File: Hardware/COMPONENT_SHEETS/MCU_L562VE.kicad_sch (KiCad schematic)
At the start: 29 parts, among them SW1 MCU Reset, U9 STM32L562VET6Q, Y2 32MHz

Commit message: wtf is wrong with my github install
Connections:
- net ABORT_1: now also U9.37 (PE9); no longer U9.62 (PD15)
- net ABORT_2: now also U9.38 (PE10); no longer U9.61 (PD14)
- net SPI1_MISO: now also U9.53 (PB14); no longer U9.30 (PA6)
- net SPI1_MOSI: now also U9.54 (PB15); no longer U9.31 (PA7)
- net SPI1_SCK: now also U9.52 (PB13); no longer U9.29 (PA5)
- net SPI2_MISO: now also U9.30 (PA6); no longer U9.53 (PB14)
- net SPI2_MOSI: now also U9.31 (PA7); no longer U9.54 (PB15)
- net SPI2_SCK: now also U9.29 (PA5); no longer U9.52 (PB13)
- net at U9.35 (PE7): no longer D2.2 (A)
- net at U9.36 (PE8): no longer D3.2 (A)
- net at D4.2 (A): no longer U9.37 (PE9)
- net at D5.2 (A): no longer U9.38 (PE10)
- net at U9.39 (PE11): no longer D6.2 (A)
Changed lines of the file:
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@@
-    (stroke (width 0) (type default) (color 0 0 0 0))
-  )
-  (wire (pts (xy 77.47 111.76) (xy 52.07 111.76))
     (stroke (width 0) (type default) (color 0 0 0 0))
   )
@@
     (stroke (width 0) (type default) (color 0 0 0 0))
   )
-  (wire (pts (xy 77.47 109.22) (xy 44.45 109.22))
-    (stroke (width 0) (type default) (color 0 0 0 0))
-  )
   (wire (pts (xy 97.79 172.72) (xy 97.79 173.99))
     (stroke (width 0) (type default) (color 0 0 0 0))
@@
     (stroke (width 0) (type default) (color 0 0 0 0))
   )
-  (wire (pts (xy 77.47 101.6) (xy 21.59 101.6))
-    (stroke (width 0) (type default) (color 0 0 0 0))
-  )
   (wire (pts (xy 102.87 33.02) (xy 102.87 31.75))
     (stroke (width 0) (type default) (color 0 0 0 0))
@@
     (stroke (width 0) (type default) (color 0 0 0 0))
   )
-  (wire (pts (xy 77.47 106.68) (xy 36.83 106.68))
-    (stroke (width 0) (type default) (color 0 0 0 0))
-  )
   (wire (pts (xy 44.45 123.19) (xy 44.45 125.73))
     (stroke (width 0) (type default) (color 0 0 0 0))
@@
   )
   (wire (pts (xy 189.23 34.29) (xy 189.23 35.56))
-    (stroke (width 0) (type default) (color 0 0 0 0))
-  )
-  (wire (pts (xy 77.47 104.14) (xy 29.21 104.14))
     (stroke (width 0) (type default) (color 0 0 0 0))
   )
@@
     (effects (font (size 1.27 1.27)) (justify left))
   )
-  (hierarchical_label "ABORT_1" (shape input) (at 77.47 165.1 180)
-    (effects (font (size 1.27 1.27)) (justify right))
-  )
-  (hierarchical_label "SPI2_MISO" (shape input) (at 123.19 119.38 0)
-    (effects (font (size 1.27 1.27)) (justify left))
-  )
-  (hierarchical_label "SPI2_SCK" (shape input) (at 123.19 116.84 0)
+  (hierarchical_label "ABORT_1" (shape input) (at 77.47 106.68 180)
+    (effects (font (size 1.27 1.27)) (justify right))
+  )
+  (hierarchical_label "SPI2_MISO" (shape input) (at 123.19 55.88 0)
+    (effects (font (size 1.27 1.27)) (justify left))
+  )
+  (hierarchical_label "SPI2_SCK" (shape input) (at 123.19 53.34 0)
     (effects (font (size 1.27 1.27)) (justify left))
   )
@@
     (effects (font (size 1.27 1.27)) (justify left))
   )
-  (hierarchical_label "ABORT_2" (shape input) (at 77.47 162.56 180)
-    (effects (font (size 1.27 1.27)) (justify right))
-  )
-  (hierarchical_label "SPI2_MOSI" (shape input) (at 123.19 121.92 0)
-    (effects (font (size 1.27 1.27)) (justify left))
-  )
-  (hierarchical_label "SPI1_MISO" (shape input) (at 123.19 55.88 0)
+  (hierarchical_label "ABORT_2" (shape input) (at 77.47 109.22 180)
+    (effects (font (size 1.27 1.27)) (justify right))
+  )
+  (hierarchical_label "SPI2_MOSI" (shape input) (at 123.19 58.42 0)
+    (effects (font (size 1.27 1.27)) (justify left))
+  )
+  (hierarchical_label "SPI1_MISO" (shape input) (at 123.19 119.38 0)
     (effects (font (size 1.27 1.27)) (justify left))
   )
@@
     (effects (font (size 1.27 1.27)) (justify left))
   )
-  (hierarchical_label "SPI1_SCK" (shape input) (at 123.19 53.34 0)
+  (hierarchical_label "SPI1_SCK" (shape input) (at 123.19 116.84 0)
     (effects (font (size 1.27 1.27)) (justify left))
   )
@@
     (effects (font (size 1.27 1.27)) (justify right))
   )
-  (hierarchical_label "SPI1_MOSI" (shape input) (at 123.19 58.42 0)
-    (effects (font (size 1.27 1.27)) (justify left))
-  )
+  (hierarchical_label "SPI1_MOSI" (shape input) (at 123.19 121.92 0)
+    (effects (font (size 1.27 1.27)) (justify left))
+  )

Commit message: almost there
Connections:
- net GND: now also D2.1 (K), D3.1 (K), D4.1 (K), D5.1 (K), D6.1 (K); no longer R10.1, R6.1, R7.1, R8.1, R9.1
- net at R10.2: no longer D6.1 (K)
- net at D6.2 (A): now also R10.1
- net at R9.2: no longer D5.1 (K)
- net at D5.2 (A): now also R9.1
- net at R8.2: no longer D4.1 (K)
- net at D4.2 (A): now also R8.1
- net at R7.2: no longer D3.1 (K)
- net at D3.2 (A): now also R7.1
- net at R6.2: no longer D2.1 (K)
- net at D2.2 (A): now also R6.1
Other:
- moved on the sheet: R10, R6, R7, R8, R9
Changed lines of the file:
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@@
-    (stroke (width 0) (type default) (color 0 0 0 0))
-  )
-  (wire (pts (xy 44.45 109.22) (xy 44.45 118.11))
     (stroke (width 0) (type default) (color 0 0 0 0))
   )
@@
     (stroke (width 0) (type default) (color 0 0 0 0))
   )
-  (wire (pts (xy 29.21 123.19) (xy 29.21 125.73))
+  (wire (pts (xy 29.21 123.19) (xy 29.21 130.81))
     (stroke (width 0) (type default) (color 0 0 0 0))
   )
@@
     (stroke (width 0) (type default) (color 0 0 0 0))
   )
-  (wire (pts (xy 52.07 118.11) (xy 52.07 111.76))
-    (stroke (width 0) (type default) (color 0 0 0 0))
-  )
   (wire (pts (xy 189.23 40.64) (xy 189.23 41.91))
     (stroke (width 0) (type default) (color 0 0 0 0))
@@
     (stroke (width 0) (type default) (color 0 0 0 0))
   )
-  (wire (pts (xy 21.59 118.11) (xy 21.59 101.6))
-    (stroke (width 0) (type default) (color 0 0 0 0))
-  )
   (wire (pts (xy 107.95 31.75) (xy 110.49 31.75))
     (stroke (width 0) (type default) (color 0 0 0 0))
@@
     (stroke (width 0) (type default) (color 0 0 0 0))
   )
-  (wire (pts (xy 21.59 123.19) (xy 21.59 125.73))
+  (wire (pts (xy 21.59 123.19) (xy 21.59 130.81))
     (stroke (width 0) (type default) (color 0 0 0 0))
   )
@@
     (stroke (width 0) (type default) (color 0 0 0 0))
   )
+  (wire (pts (xy 52.07 114.3) (xy 52.07 118.11))
+    (stroke (width 0) (type default) (color 0 0 0 0))
+  )
   (wire (pts (xy 102.87 33.02) (xy 102.87 31.75))
     (stroke (width 0) (type default) (color 0 0 0 0))
@@
     (stroke (width 0) (type default) (color 0 0 0 0))
   )
-  (wire (pts (xy 29.21 118.11) (xy 29.21 104.14))
-    (stroke (width 0) (type default) (color 0 0 0 0))
-  )
   (wire (pts (xy 95.25 31.75) (xy 97.79 31.75))
     (stroke (width 0) (type default) (color 0 0 0 0))
@@
     (stroke (width 0) (type default) (color 0 0 0 0))
   )
-  (wire (pts (xy 44.45 123.19) (xy 44.45 125.73))
+  (wire (pts (xy 44.45 123.19) (xy 44.45 130.81))
     (stroke (width 0) (type default) (color 0 0 0 0))
   )
@@
     (stroke (width 0) (type default) (color 0 0 0 0))
   )
+  (wire (pts (xy 44.45 114.3) (xy 44.45 118.11))
+    (stroke (width 0) (type default) (color 0 0 0 0))
+  )
   (wire (pts (xy 223.52 40.64) (xy 223.52 41.91))
     (stroke (width 0) (type default) (color 0 0 0 0))
@@
     (stroke (width 0) (type default) (color 0 0 0 0))
   )
-  (wire (pts (xy 36.83 123.19) (xy 36.83 125.73))
+  (wire (pts (xy 36.83 114.3) (xy 36.83 118.11))
+    (stroke (width 0) (type default) (color 0 0 0 0))
+  )
+  (wire (pts (xy 36.83 123.19) (xy 36.83 130.81))
     (stroke (width 0) (type default) (color 0 0 0 0))
   )
@@
     (stroke (width 0) (type default) (color 0 0 0 0))
   )
-  (wire (pts (xy 52.07 123.19) (xy 52.07 125.73))
+  (wire (pts (xy 52.07 123.19) (xy 52.07 130.81))
     (stroke (width 0) (type default) (color 0 0 0 0))
   )
@@
     (stroke (width 0) (type default) (color 0 0 0 0))
   )
-  (wire (pts (xy 36.83 118.11) (xy 36.83 106.68))
+  (wire (pts (xy 21.59 114.3) (xy 21.59 118.11))
     (stroke (width 0) (type default) (color 0 0 0 0))
   )
@@
   )
   (wire (pts (xy 90.17 31.75) (xy 90.17 33.02))
+    (stroke (width 0) (type default) (color 0 0 0 0))
+  )
+  (wire (pts (xy 29.21 114.3) (xy 29.21 118.11))
     (stroke (width 0) (type default) (color 0 0 0 0))
   )
@@
     (pin "2")
   )
-  (symbol (lib_id "Device:R_Small") (at 21.59 128.27 180) (unit 1)
-    (in_bom yes) (on_board yes)
-    (property "Reference" "R6" (id 0) (at 24.13 129.54 0))
-    (property "Value" "820" (id 1) (at 25.4 127 0))
-    (property "Footprint" "Resistor_SMD:R_0603_1608Metric_Pad0.98x0.95mm_HandSolder" (id 2) (at 21.59 128.27 0)
-      (effects (font (size 1.27 1.27)) hide)
-    )
-    (property "Datasheet" "~" (id 3) (at 21.59 128.27 0)
-      (effects (font (size 1.27 1.27)) hide)
-    )
-    (property "LCSC" " C23253" (id 4) (at 21.59 128.27 0)
-      (effects (font (size 1.27 1.27)) hide)
-    )
-    (pin "1")
-    (pin "2")
-  )
-  (symbol (lib_id "Device:R_Small") (at 36.83 128.27 180) (unit 1)
-    (in_bom yes) (on_board yes)
-    (property "Reference" "R8" (id 0) (at 39.37 129.54 0))
-    (property "Value" "820" (id 1) (at 40.64 127 0))
-    (property "Footprint" "Resistor_SMD:R_0603_1608Metric_Pad0.98x0.95mm_HandSolder" (id 2) (at 36.83 128.27 0)
-      (effects (font (size 1.27 1.27)) hide)
-    )
-    (property "Datasheet" "~" (id 3) (at 36.83 128.27 0)
-      (effects (font (size 1.27 1.27)) hide)
-    )
-    (property "LCSC" " C23253 " (id 4) (at 36.83 128.27 0)
-      (effects (font (size 1.27 1.27)) hide)
-    )
-    (pin "1")
-    (pin "2")
-  )
-  (symbol (lib_id "Device:R_Small") (at 52.07 128.27 180) (unit 1)
-    (in_bom yes) (on_board yes)
-    (property "Reference" "R10" (id 0) (at 55.88 129.54 0))
-    (property "Value" "820" (id 1) (at 55.88 127 0))
-    (property "Footprint" "Resistor_SMD:R_0603_1608Metric_Pad0.98x0.95mm_HandSolder" (id 2) (at 52.07 128.27 0)
-      (effects (font (size 1.27 1.27)) hide)
-    )
-    (property "Datasheet" "~" (id 3) (at 52.07 128.27 0)
-      (effects (font (size 1.27 1.27)) hide)
-    )
-    (property "LCSC" " C23253 " (id 4) (at 52.07 128.27 0)
-      (effects (font (size 1.27 1.27)) hide)
-    )
-    (pin "1")
-    (pin "2")
-  )
-  (symbol (lib_id "Device:R_Small") (at 29.21 128.27 180) (unit 1)
-    (in_bom yes) (on_board yes)
-    (property "Reference" "R7" (id 0) (at 31.75 129.54 0))
-    (property "Value" "820" (id 1) (at 33.02 127 0))
-    (property "Footprint" "Resistor_SMD:R_0603_1608Metric_Pad0.98x0.95mm_HandSolder" (id 2) (at 29.21 128.27 0)
-      (effects (font (size 1.27 1.27)) hide)
-    )
-    (property "Datasheet" "~" (id 3) (at 29.21 128.27 0)
-      (effects (font (size 1.27 1.27)) hide)
-    )
-    (property "LCSC" " C23253 " (id 4) (at 29.21 128.27 0)
-      (effects (font (size 1.27 1.27)) hide)
-    )
-    (pin "1")
-    (pin "2")
-  )
-  (symbol (lib_id "Device:R_Small") (at 44.45 128.27 180) (unit 1)
-    (in_bom yes) (on_board yes)
-    (property "Reference" "R9" (id 0) (at 46.99 129.54 0))
-    (property "Value" "820" (id 1) (at 48.26 127 0))
-    (property "Footprint" "Resistor_SMD:R_0603_1608Metric_Pad0.98x0.95mm_HandSolder" (id 2) (at 44.45 128.27 0)
-      (effects (font (size 1.27 1.27)) hide)
-    )
-    (property "Datasheet" "~" (id 3) (at 44.45 128.27 0)
-      (effects (font (size 1.27 1.27)) hide)
-    )
-    (property "LCSC" " C23253 " (id 4) (at 44.45 128.27 0)
-      (effects (font (size 1.27 1.27)) hide)
-    )
+  (symbol (lib_id "Device:R_Small") (at 21.59 111.76 180) (unit 1)
+    (in_bom yes) (on_board yes)
+    (property "Reference" "R6" (id 0) (at 24.13 113.03 0))
+    (property "Value" "820" (id 1) (at 25.4 110.49 0))
+    (property "Footprint" "Resistor_SMD:R_0603_1608Metric_Pad0.98x0.95mm_HandSolder" (id 2) (at 21.59 111.76 0)
+      (effects (font (size 1.27 1.27)) hide)
+    )
+    (property "Datasheet" "~" (id 3) (at 21.59 111.76 0)
+      (effects (font (size 1.27 1.27)) hide)
+    )
+    (property "LCSC" " C23253" (id 4) (at 21.59 111.76 0)
+      (effects (font (size 1.27 1.27)) hide)
+    )
+    (pin "1")
+    (pin "2")
+  )
+  (symbol (lib_id "Device:R_Small") (at 36.83 111.76 180) (unit 1)
+    (in_bom yes) (on_board yes)
+    (property "Reference" "R8" (id 0) (at 39.37 113.03 0))
+    (property "Value" "820" (id 1) (at 40.64 110.49 0))
+    (property "Footprint" "Resistor_SMD:R_0603_1608Metric_Pad0.98x0.95mm_HandSolder" (id 2) (at 36.83 111.76 0)
+      (effects (font (size 1.27 1.27)) hide)
+    )
+    (property "Datasheet" "~" (id 3) (at 36.83 111.76 0)
+      (effects (font (size 1.27 1.27)) hide)
+    )
+    (property "LCSC" " C23253 " (id 4) (at 36.83 111.76 0)
+      (effects (font (size 1.27 1.27)) hide)
+    )
+    (pin "1")
+    (pin "2")
+  )
+  (symbol (lib_id "Device:R_Small") (at 52.07 111.76 180) (unit 1)
+    (in_bom yes) (on_board yes)
+    (property "Reference" "R10" (id 0) (at 55.88 113.03 0))
+    (property "Value" "820" (id 1) (at 55.88 110.49 0))
+    (property "Footprint" "Resistor_SMD:R_0603_1608Metric_Pad0.98x0.95mm_HandSolder" (id 2) (at 52.07 111.76 0)
+      (effects (font (size 1.27 1.27)) hide)
+    )
+    (property "Datasheet" "~" (id 3) (at 52.07 111.76 0)
+      (effects (font (size 1.27 1.27)) hide)
+    )
+    (property "LCSC" " C23253 " (id 4) (at 52.07 111.76 0)
+      (effects (font (size 1.27 1.27)) hide)
+    )
+    (pin "1")
+    (pin "2")
+  )
+  (symbol (lib_id "Device:R_Small") (at 29.21 111.76 180) (unit 1)
+    (in_bom yes) (on_board yes)
+    (property "Reference" "R7" (id 0) (at 31.75 113.03 0))
+    (property "Value" "820" (id 1) (at 33.02 110.49 0))
+    (property "Footprint" "Resistor_SMD:R_0603_1608Metric_Pad0.98x0.95mm_HandSolder" (id 2) (at 29.21 111.76 0)
+      (effects (font (size 1.27 1.27)) hide)
+    )
+    (property "Datasheet" "~" (id 3) (at 29.21 111.76 0)
+      (effects (font (size 1.27 1.27)) hide)
+    )
+    (property "LCSC" " C23253 " (id 4) (at 29.21 111.76 0)
+      (effects (font (size 1.27 1.27)) hide)
+    )
+    (pin "1")
+    (pin "2")
+  )
+  (symbol (lib_id "Device:R_Small") (at 44.45 111.76 180) (unit 1)
+    (in_bom yes) (on_board yes)
+    (property "Reference" "R9" (id 0) (at 46.99 113.03 0))
+    (property "Value" "820" (id 1) (at 48.26 110.49 0))
+    (property "Footprint" "Resistor_SMD:R_0603_1608Metric_Pad0.98x0.95mm_HandSolder" (id 2) (at 44.45 111.76 0)
+      (effects (font (size 1.27 1.27)) hide)
+    )
+    (property "Datasheet" "~" (id 3) (at 44.45 111.76 0)
+      (effects (font (size 1.27 1.27)) hide)
+    )
+    (property "LCSC" " C23253 " (id 4) (at 44.45 111.76 0)
+      (effects (font (size 1.27 1.27)) hide)
+    )

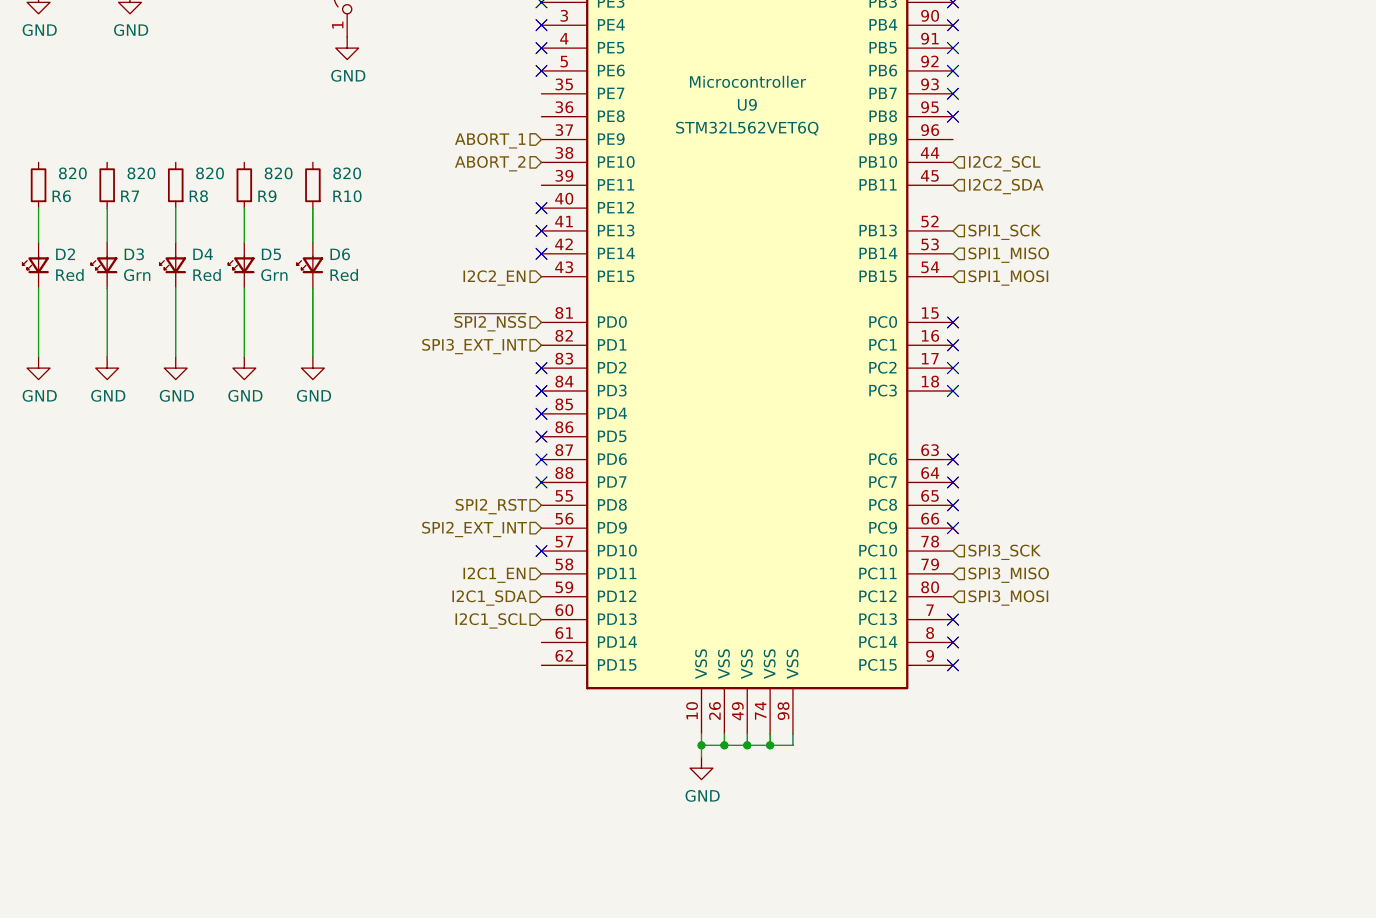
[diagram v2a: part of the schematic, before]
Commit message: Replaced Temp Sense and finalized routing
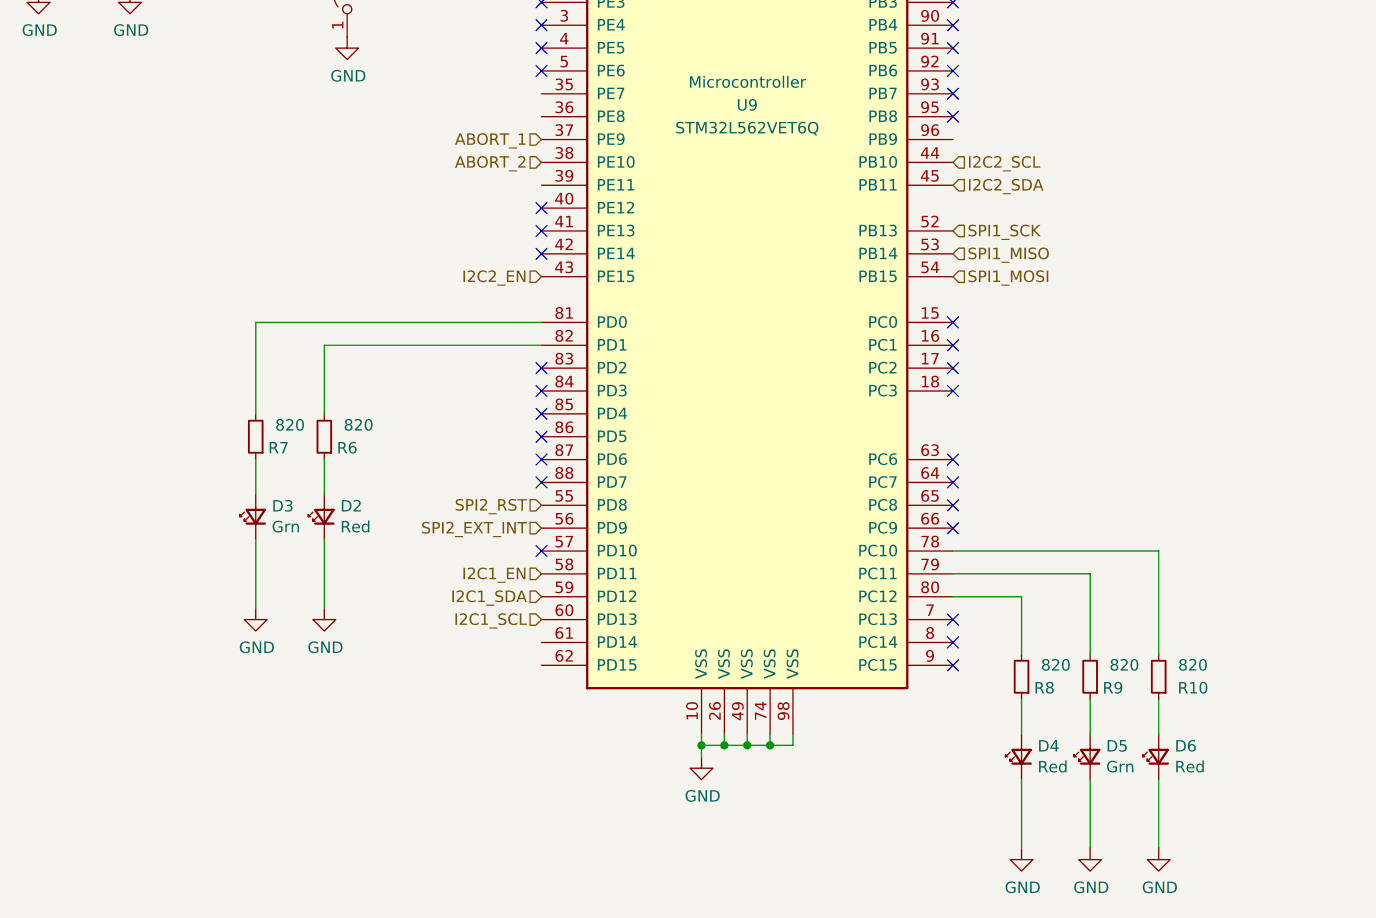
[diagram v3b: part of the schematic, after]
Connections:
- net SPI3_EXT_INT is gone; now on an unnamed net: U9.82 (PD1)
- net SPI3_MISO is gone; now on an unnamed net: U9.79 (PC11)
- net SPI3_MOSI is gone; now on an unnamed net: U9.80 (PC12)
- net SPI3_SCK is gone; now on an unnamed net: U9.78 (PC10)
- net ~{SPI2_NSS} is gone; now on an unnamed net: U9.81 (PD0)
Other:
- moved on the sheet: D2, D3, D4, D5, D6, R10, R6, R7, R8, R9
